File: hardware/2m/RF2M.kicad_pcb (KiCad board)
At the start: 2 copper layers, 180 x 140 mm, 326 parts, among them J101 Controller 20 pin, J301 Protected pack JST VH, J302 Exclusive converter link, J501 NORMAL 50ohm SMA, J701 TRAIN MMCX 50ohm, Q301 2N7002, Q302 AO3401A, Q303 MMBT3904,215, Q305 AO3401A, Q306 MMBT3904,215, Q309 AO3401A, Q401 D45H11, Q402 BD139, Q403 MMBT3904,215, Q404 MMBT3904,215, Q405 MMBT3904,215, Q501 PD54008L-E, Q502 2N7002, Q701 MMBTH10LT1G, Q702 MMBT3904,215, Q703 MMBT3904,215, Q704 MMBT3904,215, U101 TPS22919DCKR, U102 SN74LVC2G66DCUR, U103 Si5351A-B-GT, U201 TPS3431SDRBR, U202 74HC174D,653, U203 74HC14D,653, U204 74HC11D,653, U205 74HC21D,653, U206 74HC11D,653, U207 74HC32D,653, U208 TLV803EA29DBZR, U301 TPS54302DDCR, U302 TPS611781RNWR, U303 TLV76150DCYR, U304 SN74LVC2G08DCUR, U305 TPS22810DBVR, U401 TLV9004IDR, U402 SN74LVC1G3157DBVR, U501 PHA-1+, U601 SN74LVC1G125DBVR, U701 SN74LVC1G125DBVR, U801 TL431BIDBZR, U802 LM339BDR, U803 LM339BDR, U804 INA180A1IDBVR, U950 TLV76701DRVR, Y101 25MHz CL10p 10/10ppm

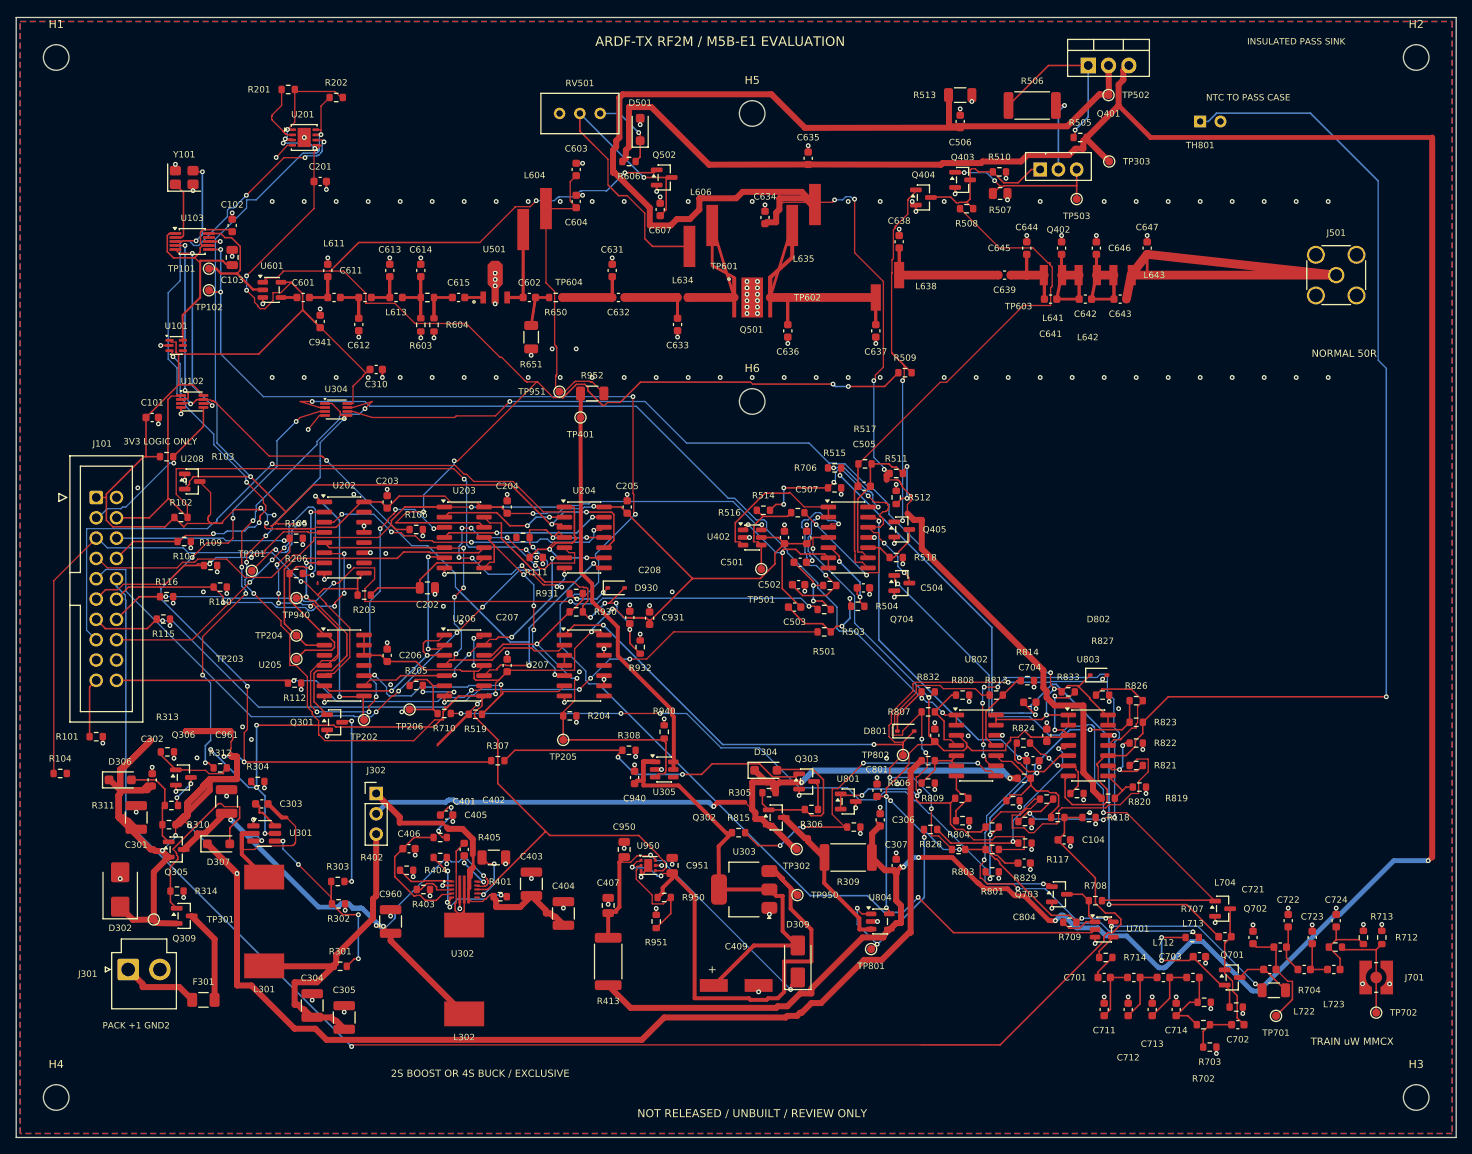
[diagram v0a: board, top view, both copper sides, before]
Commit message: Correct RF2M copper geometry and prepare M5B-E2 manufacturing review
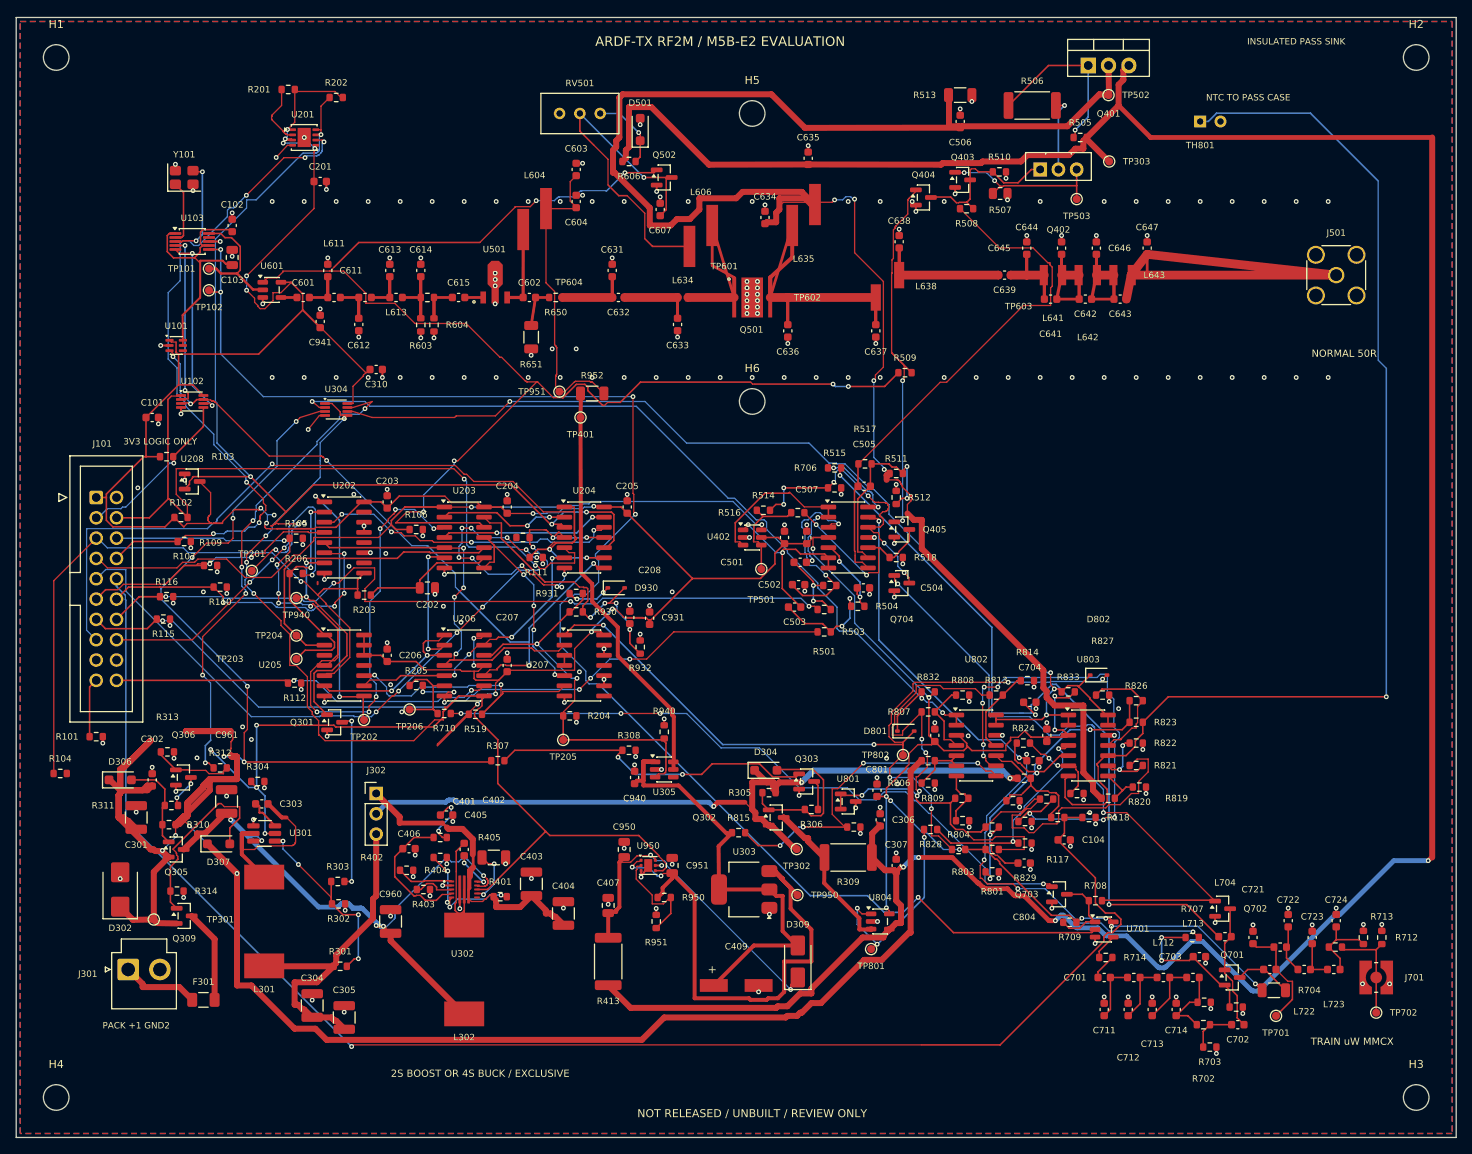
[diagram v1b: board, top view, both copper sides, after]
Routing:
- net PACK_OK_N: track 112.4 -> 109.5 mm
- net V3V3: track 485.1 -> 484.4 mm
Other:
- board text added: "ARDF-TX RF2M / M5B-E2 EVALUATION"
- board text removed: "ARDF-TX RF2M / M5B-E1 EVALUATION"
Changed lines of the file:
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@@
 		(title "RF2M 144MHz TRUE-AM INTEGRATED EVALUATION")
 		(date "2026-10-16")
-		(rev "M5B-E1")
+		(rev "M5B-E2")
 		(company "ARDF-TX")
 		(comment 1 "NOT RELEASED / UNBUILT / REVIEW FILES ONLY")
@@
 		)
 	)
-	(gr_text "ARDF-TX RF2M / M5B-E1 EVALUATION"
+	(gr_text "ARDF-TX RF2M / M5B-E2 EVALUATION"
 		(at 108 23 0)
 		(layer "F.SilkS")
@@
 	(segment
 		(start 57.225 36.85)
-		(end 58.1 35.975)
+		(end 57.45 35.975)
 		(width 0.15)
 		(layer "F.Cu")
@@
 	)
 	(segment
+		(start 174.9 140.8)
+		(end 175.5 141.1)
+		(width 0.3)
+		(layer "F.Cu")
+		(net "V3V3")
+	)
+	(segment
 		(start 54.3519 53.1)
 		(end 55.8046 54.5527)
@@
 	)
 	(segment
-		(start 57.325 36.1)
-		(end 57.45 35.975)
-		(width 0.15)
-		(layer "F.Cu")
-		(net "V3V3")
-	)
-	(segment
 		(start 39.387 60.5745)
 		(end 39.1625 60.35)
@@
 	)
 	(segment
-		(start 57.45 35.975)
-		(end 58.1 35.975)
-		(width 0.15)
-		(locked yes)
-		(layer "F.Cu")
-		(net "V3V3")
-	)
-	(segment
 		(start 135.955 111.635)
 		(end 134.825 110.505)
@@
 	)
 	(segment
-		(start 57.325 36.375)
-		(end 57.325 36.1)
-		(width 0.15)
-		(layer "F.Cu")
-		(net "V3V3")
-	)
-	(segment
 		(start 138.4445 111.635)
 		(end 135.955 111.635)
@@
 		(start 63.7 64.4)
 		(end 63.8 64.4)
-		(width 0.15)
+		(width 0.2)
 		(layer "F.Cu")
 		(net "V3V3")
@@
 	)
 	(segment
-		(start 128.3 82.7)
-		(end 128.3 82.6)
-		(width 0.15)
-		(layer "F.Cu")
-		(net "TRAIN_COMMAND")
-	)
-	(segment
 		(start 128.675 81.75)
 		(end 128.699999 81.725)
@@
 	)
 	(segment
-		(start 128.1 82.5)
-		(end 128.1 82.4)
-		(width 0.15)
-		(layer "F.Cu")
-		(net "TRAIN_COMMAND")
-	)
-	(segment
 		(start 128.824999 80.725)
 		(end 128.8 80.725)
@@
 	)
 	(segment
-		(start 128.199999 82.5)
-		(end 128.1 82.5)
-		(width 0.15)
-		(layer "F.Cu")
-		(net "TRAIN_COMMAND")
-	)
-	(segment
 		(start 128.625 80.65)
 		(end 128.6 80.625)
@@
 	(segment
 		(start 128.4 82.7)
-		(end 128.3 82.7)
-		(width 0.15)
+		(end 128.1 82.4)
+		(width 0.2)
 		(layer "F.Cu")
 		(net "TRAIN_COMMAND")
@@
 	(segment
 		(start 57.9 68.75)
-		(end 55.5 68)
+		(end 57 68)
 		(width 0.15)
 		(locked yes)
@@
 		(net "PACK_OK_N")
 	)
-	(segment
-		(start 55.5 68)
-		(end 57 68)
-		(width 0.15)
-		(layer "F.Cu")
-		(net "PACK_OK_N")
-	)
 	(via
 		(at 135.8 106.9)
@@
 			)
 		)
+	)
+	(zone
+		(layer "F.Cu")
+		(hatch edge 0.5)
+		(connect_pads
+			(clearance 0)
+		)
+		(min_thickness 0.25)
+		(keepout
+			(tracks allowed)
+			(vias allowed)
+			(pads allowed)
+			(copperpour not_allowed)
+			(footprints allowed)
+		)
+		(placement
+			(enabled no)
+			(sheetname "")
+		)
+		(fill
+			(thermal_gap 0.5)
+			(thermal_bridge_width 0.5)
+			(island_removal_mode 0)
+		)
+		(polygon
+			(pts
+				(xy 128 126.9) (xy 128.4 126.9) (xy 128.4 127.3) (xy 128 127.3)
+			)
+		)

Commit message: Implement M5B-E3 standard JLCPCB RF2M evaluation board
Recalculate and implement 1.6 mm / 1 oz RF geometry, power copper, thermal vias, connector holes and manufacturing legend. Preserve electrical functions and population variants. Add native-geometry DFM, regression checks and fresh native/fabrication review archives. CAD milestone only; no manufacturing or operational release.
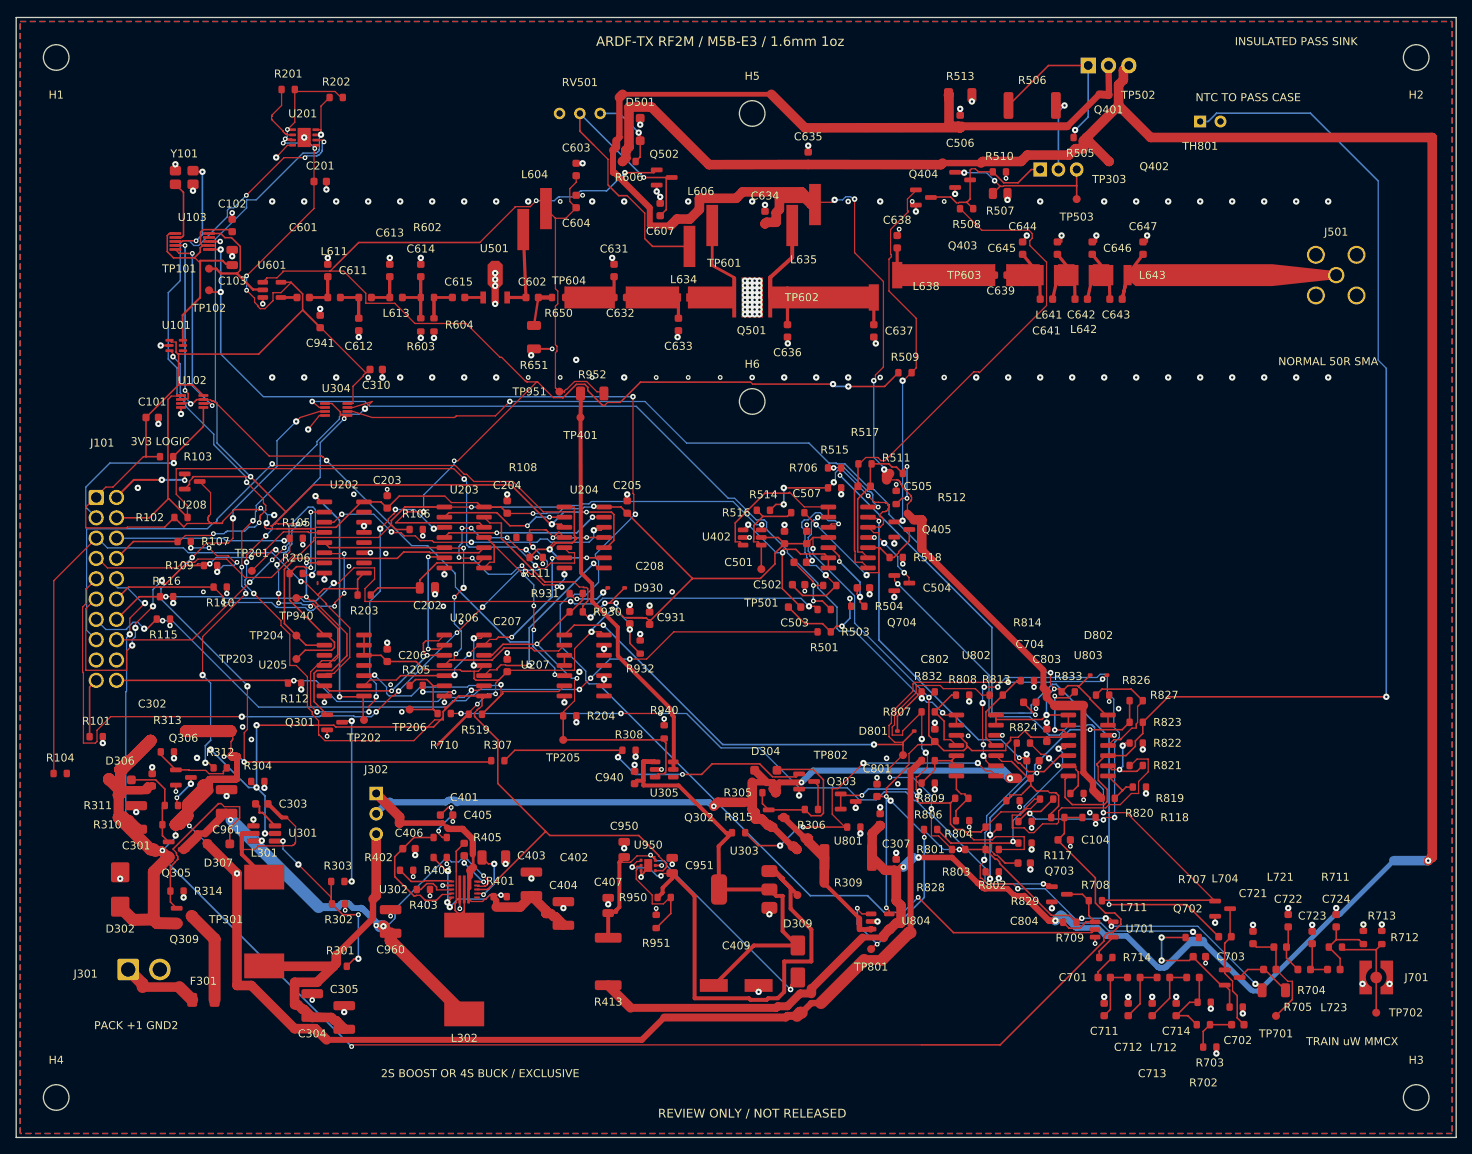
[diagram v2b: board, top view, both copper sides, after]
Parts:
- C101, C102, C104, C201, C203, C204, C205, C206, C207, C208, C302, C303, C306, C307, C310, C401, C405, C406, C501, C502, C503, C504, C505, C506, C507, C508, C601, C602, C603, C604, C607, C611, C612, C613, C614, C615, C631, C632, C633, C634, C635, C636, C637, C638, C639, C641, C642, C643, C644, C645, C646, C647, C701, C702, C703, C704, C705, C706, C711, C712, C713, C714, C721, C722, C723, C724, C801, C802, C803, C804, C931, C940, C941: footprint Capacitor_SMD:C_0603_1608Metric -> ARDF_2M:C_0603_1608Metric_E3
- C103, C202, C407, C950, C951: footprint Capacitor_SMD:C_0805_2012Metric -> ARDF_2M:C_0805_2012Metric_E3
- C301, C304, C305, C403, C404, C960, C961: footprint Capacitor_SMD:C_1210_3225Metric -> ARDF_2M:C_1210_3225Metric_E3
- C402: footprint Capacitor_SMD:C_1206_3216Metric -> ARDF_2M:C_1206_3216Metric_E3
- D302: footprint Diode_SMD:D_SMB -> ARDF_2M:D_SMB_E3
- D304, D306, D307, D501: footprint Diode_SMD:D_SOD-123F -> ARDF_2M:D_SOD-123F_E3
- D309: footprint Diode_SMD:D_SMA -> ARDF_2M:D_SMA_E3
- D801, D802, D930: footprint Diode_SMD:D_SOD-323 -> ARDF_2M:D_SOD-323_E3
- F301: footprint Fuse:Fuse_1206_3216Metric -> ARDF_2M:Fuse_1206_3216Metric_E3
- H1, H2, H3, H4, H5, H6: footprint MountingHole_3.2mm_M3 -> ARDF_2M:MountingHole_3.2mm_M3_E3
- J301: footprint Connector_JST:JST_VH_B2P-VH_1x02_P3.96mm_Vertical -> ARDF_2M:JST_VH_B2P-VH_1x02_P3.96mm_Vertical_E3
- J302: footprint Connector_PinHeader_2.54mm:PinHeader_1x03_P2.54mm_Vertical -> ARDF_2M:PinHeader_1x03_P2.54mm_Vertical_E3
- J501: footprint Connector_Coaxial:SMA_Amphenol_132134_Vertical -> ARDF_2M:SMA_Amphenol_132134_Vertical_E3
- J701: footprint Connector_Coaxial:WR-MMCX_Wuerth_66012102111404_Vertical -> ARDF_2M:WR-MMCX_Wuerth_66012102111404_Vertical_E3
- L611, L612, L613, L704, L711, L712, L713, L721, L722, L723: footprint Inductor_SMD:L_0603_1608Metric -> ARDF_2M:L_0603_1608Metric_E3
- Q301, Q302, Q303, Q305, Q306, Q309, Q403, Q404, Q405, Q502, Q701, Q702, Q703, Q704, U208, U801: footprint Package_TO_SOT_SMD:SOT-23 -> ARDF_2M:SOT-23_E3
- Q401: footprint Package_TO_SOT_THT:TO-220-3_Vertical -> ARDF_2M:TO-220-3_Vertical_E3
- Q402: footprint Package_TO_SOT_THT:TO-126-3_Vertical -> ARDF_2M:TO-126-3_Vertical_E3
- R101, R102, R103, R104, R105, R106, R107, R108, R109, R110, R111, R112, R115, R116, R117, R118, R201, R202, R203, R204, R205, R206, R301, R302, R303, R304, R305, R306, R307, R308, R310, R311, R312, R313, R314, R401, R402, R403, R404, R405, R501, R502, R503, R504, R505, R508, R509, R510, R511, R512, R514, R515, R516, R517, R518, R519, R602, R603, R604, R606, R650, R702, R703, R705, R706, R707, R708, R709, R710, R711, R712, R713, R714, R715, R801, R802, R803, R804, R805, R806, R807, R808, R809, R810, R811, R812, R813, R814, R815, R816, R817, R818, R819, R820, R821, R822, R823, R824, R825, R826, R827, R828, R829, R832, R833, R930, R931, R932, R940, R950, R951: footprint Resistor_SMD:R_0603_1608Metric -> ARDF_2M:R_0603_1608Metric_E3
- R309, R413, R506: footprint Resistor_SMD:R_2512_6332Metric -> ARDF_2M:R_2512_6332Metric_E3
- R507: footprint Resistor_SMD:R_0805_2012Metric -> ARDF_2M:R_0805_2012Metric_E3
- R513, R651, R704, R952: footprint Resistor_SMD:R_1206_3216Metric -> ARDF_2M:R_1206_3216Metric_E3
- RV501: footprint Potentiometer_THT:Potentiometer_Bourns_3296W_Vertical -> ARDF_2M:Potentiometer_Bourns_3296W_Vertical_E3
- TL603: value 50R 6.23mm -> 50R 6.1129mm; footprint ARDF_2M:TL50_6p23mm -> ARDF_2M:TL50_E3_6p1129mm
- TL604: value 50R 6.62mm -> 50R 6.4956mm; footprint ARDF_2M:TL50_6p62mm -> ARDF_2M:TL50_E3_6p4956mm
- TL605: value 50R 5.8mm -> 50R 5.691mm; footprint ARDF_2M:TL50_5p8mm -> ARDF_2M:TL50_E3_5p691mm
- TL606: value 50R 2.2mm -> 50R 2.1587mm; footprint ARDF_2M:TL50_2p2mm -> ARDF_2M:TL50_E3_2p1587mm
- TL607: value 50R 11mm -> 50R 10.7933mm; footprint ARDF_2M:TL50_11p0mm -> ARDF_2M:TL50_E3_10p7933mm
- TL608: value 50R 12.4mm -> 50R 12.167mm; footprint ARDF_2M:TL50_12p4mm -> ARDF_2M:TL50_E3_12p167mm
- TL609: value 50R 2mm -> 50R 1.9624mm; footprint ARDF_2M:TL50_2p0mm -> ARDF_2M:TL50_E3_1p9624mm
- TP101, TP102, TP201, TP202, TP203, TP204, TP205, TP206, TP301, TP302, TP303, TP401, TP501, TP502, TP503, TP701, TP702, TP801, TP802, TP940, TP950, TP951: footprint TestPoint:TestPoint_Pad_D1.0mm -> ARDF_2M:TestPoint_Pad_D1.0mm_E3
- U101: footprint Package_TO_SOT_SMD:SOT-363_SC-70-6 -> ARDF_2M:SOT-363_SC-70-6_E3
- U102, U304: footprint Package_SO:VSSOP-8_2.3x2mm_P0.5mm -> ARDF_2M:VSSOP-8_2.3x2mm_P0.5mm_E3
- U103: footprint Package_SO:MSOP-10_3x3mm_P0.5mm -> ARDF_2M:MSOP-10_3x3mm_P0.5mm_E3
- U201: footprint Package_SON:VSON-8-1EP_3x3mm_P0.65mm_EP1.65x2.4mm -> ARDF_2M:VSON-8-1EP_3x3mm_P0.65mm_EP1.65x2.4mm_E3
- U202: footprint Package_SO:SOIC-16_3.9x9.9mm_P1.27mm -> ARDF_2M:SOIC-16_3.9x9.9mm_P1.27mm_E3
- U203, U204, U205, U206, U207, U401, U802, U803: footprint Package_SO:SOIC-14_3.9x8.7mm_P1.27mm -> ARDF_2M:SOIC-14_3.9x8.7mm_P1.27mm_E3
- U301: footprint Package_TO_SOT_SMD:SOT-23-6_Handsoldering -> ARDF_2M:SOT-23-6_Handsoldering_E3
- U303: footprint Package_TO_SOT_SMD:SOT-223-3_TabPin2 -> ARDF_2M:SOT-223-3_TabPin2_E3
- U305, U402: footprint Package_TO_SOT_SMD:SOT-23-6 -> ARDF_2M:SOT-23-6_E3
- U601, U701, U804: footprint Package_TO_SOT_SMD:SOT-23-5 -> ARDF_2M:SOT-23-5_E3
- U950: footprint Package_SON:WSON-6-1EP_2x2mm_P0.65mm_EP1x1.6mm -> ARDF_2M:WSON-6-1EP_2x2mm_P0.65mm_EP1x1.6mm_E3
- Y101: footprint Crystal:Crystal_SMD_3225-4Pin_3.2x2.5mm -> ARDF_2M:Crystal_SMD_3225-4Pin_3.2x2.5mm_E3
- moved C643 0.52 mm to (157.5, 55.2)
- moved C647 0.52 mm to (160.9, 48.8)
- moved C641 0.52 mm to (148.8, 55.2)
- moved C642 0.52 mm to (153.1, 55.2)
- moved C644 0.52 mm to (145.8, 48.8)
- moved C645 0.52 mm to (150.2, 48.8)
- moved C646 0.52 mm to (154.5, 48.8)
- moved L641 0.52 mm to (149.1, 52.2)
- moved L642 0.52 mm to (153.4, 52.2)
- moved L643 0.52 mm to (157.8, 52.2)
- moved C639 0.48 mm to (143.1, 52.2)
- moved TL609 0.48 mm to (143.8, 52.2)
- moved C602 0.35 mm to (84.5, 55.0)
- moved R650 0.35 mm to (87.8, 55.0)
- moved TL603 0.35 mm to (88.6, 55.0)
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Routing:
- net NORMAL_RF: track 61.4 -> 35.5 mm
- net GND: track 184.0 -> 205.7 mm, vias 279 -> 302
- net PATH_TRAIN: track 34.8 -> 53.7 mm, vias 2 -> 6
- net MUTE_N: track 91.3 -> 106.7 mm, vias 7 -> 8
- net ST_F2: track 21.5 -> 11.5 mm
- net ST_F1: track 21.5 -> 11.5 mm
- net PA_GATE: track 21.3 -> 11.9 mm
- net PA_DRAIN: track 20.6 -> 11.2 mm
- net ST_LPF_IN: track 16.6 -> 8.99 mm
- net I2C_SDA: track 21.1 -> 25.6 mm
- net V3V3: track 484.4 -> 488.0 mm
- net MMIC_COUPLED: track 8.79 -> 5.24 mm
- net ST_O_C: track 6.80 -> 3.40 mm
- net ST_O_B: track 6.80 -> 3.40 mm
- net ST_O_A: track 6.80 -> 3.40 mm
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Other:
- board text added: "3V3 LOGIC"
- board text added: "ARDF-TX RF2M / M5B-E3 / 1.6mm 1oz"
- board text added: "C802"
- board text added: "C803"
- board text added: "H1"
- board text added: "H2"
- board text added: "H3"
- board text added: "H4"
- board text added: "H5"
- board text added: "H6"
- board text added: "L711"
- board text added: "L721"
- board text added: "NORMAL 50R SMA"
- board text added: "R108"
- board text added: "R602"
- board text added: "R705"
- board text added: "R711"
- board text added: "R802"
- board text added: "REVIEW ONLY / NOT RELEASED"
- board text removed: "3V3 LOGIC ONLY"
- board text removed: "ARDF-TX RF2M / M5B-E2 EVALUATION"
- board text removed: "C306"
- board text removed: "L713"
- board text removed: "L722"
- board text removed: "NORMAL 50R"
- board text removed: "NOT RELEASED / UNBUILT / REVIEW ONLY"
- board text removed: "Q701"
- board text removed: "TP302"
- board text removed: "TP950"

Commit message: Implement M5B-E4 thermal candidate with source-joint assembly hold
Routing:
- net GND: vias 302 -> 374
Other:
- board text added: "ARDF-TX RF2M / M5B-E4 / 1.6mm 1oz"
- board text removed: "ARDF-TX RF2M / M5B-E3 / 1.6mm 1oz"
